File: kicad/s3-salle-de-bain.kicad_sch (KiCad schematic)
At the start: 22 parts, among them J1 Jack 3.5mm PJ320E, J2 USB-C, Q1 AO3401, SW1 Encodeur EC11, SW2 Switch mute, U1 ESP32-S3-DevKitC-1, U2 PCM5102 DAC, U3 PAM8403, U4 INMP441, U5 AMS1117-3.3

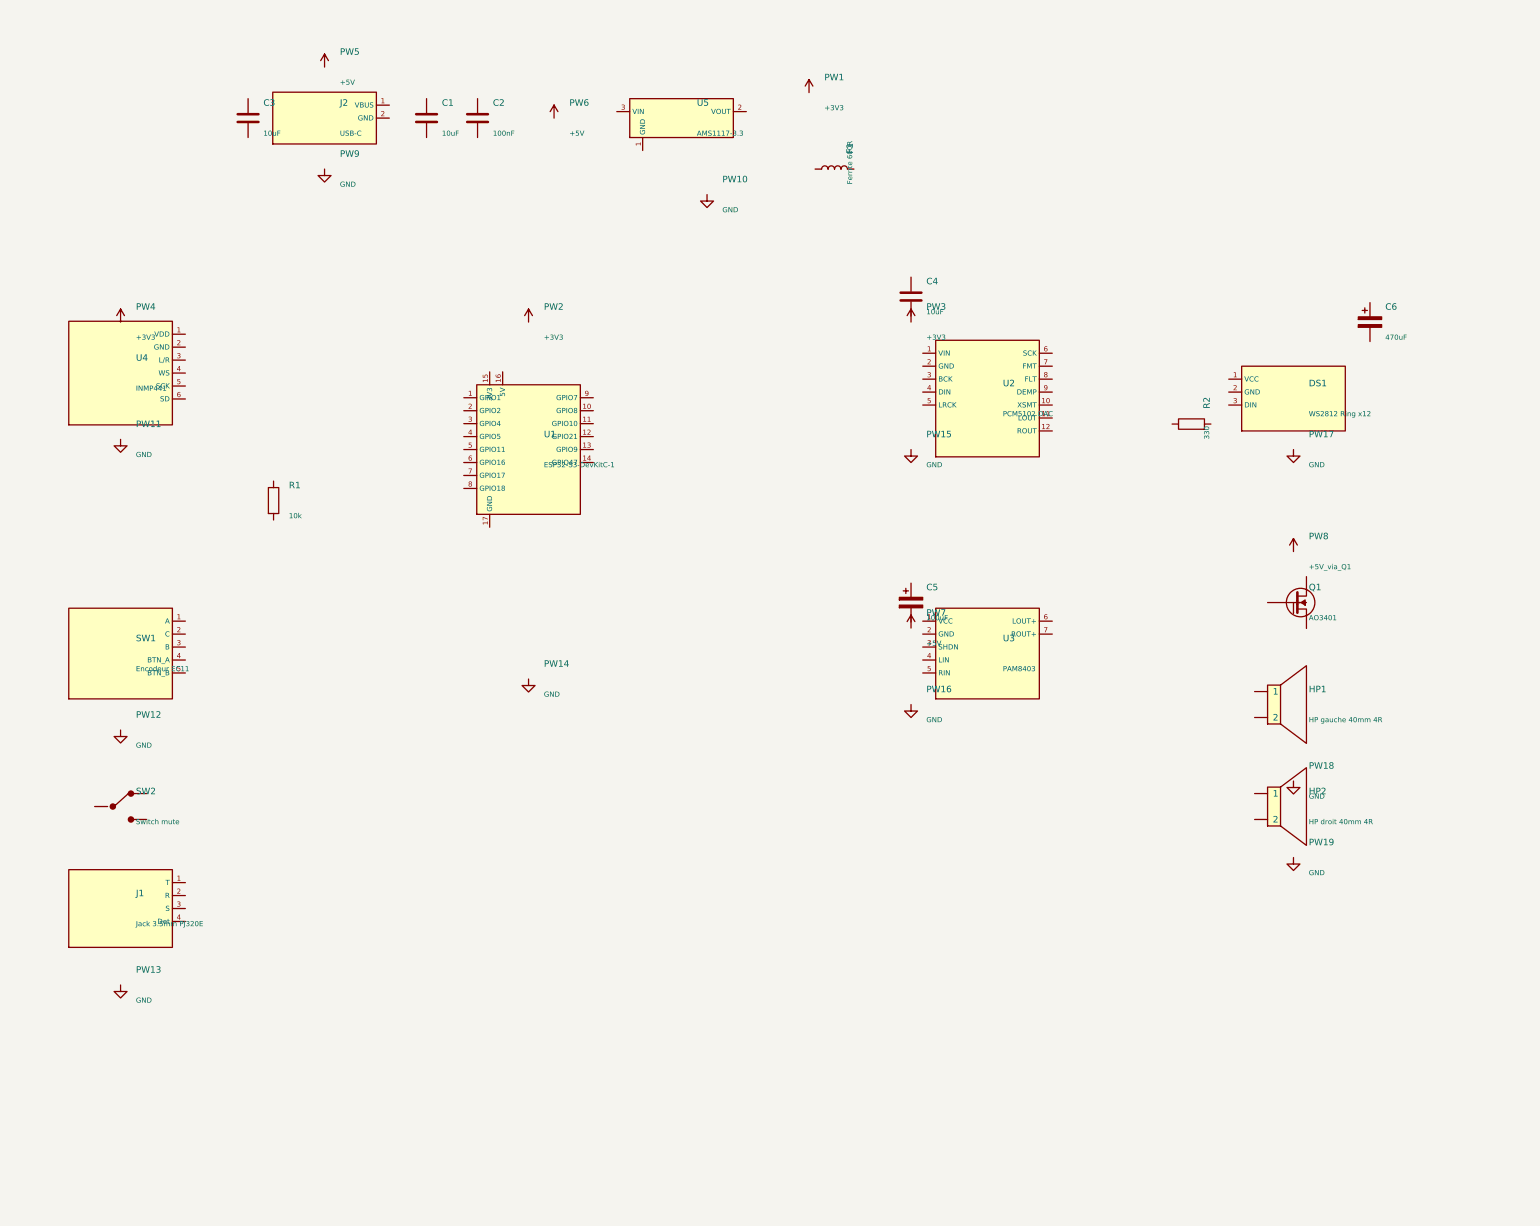
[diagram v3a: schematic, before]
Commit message: fix(kicad): real standard symbols (R/C/L/Q_PMOS/Speaker/power) + clean wiring
- Extract exact symbols from KiCad 10 libs (no lib_symbol_mismatch)
- Parse real pin positions (no off-grid, no unconnected endpoints)
- Grid-snapped placement, PWR_FLAG on each rail
- ERC: 216 -> 19 warnings (only cosmetic Local-lib notices)
- Verified with kicad-cli erc/pdf/svg export
- Official netlist: 24 nets, 22 components all connected
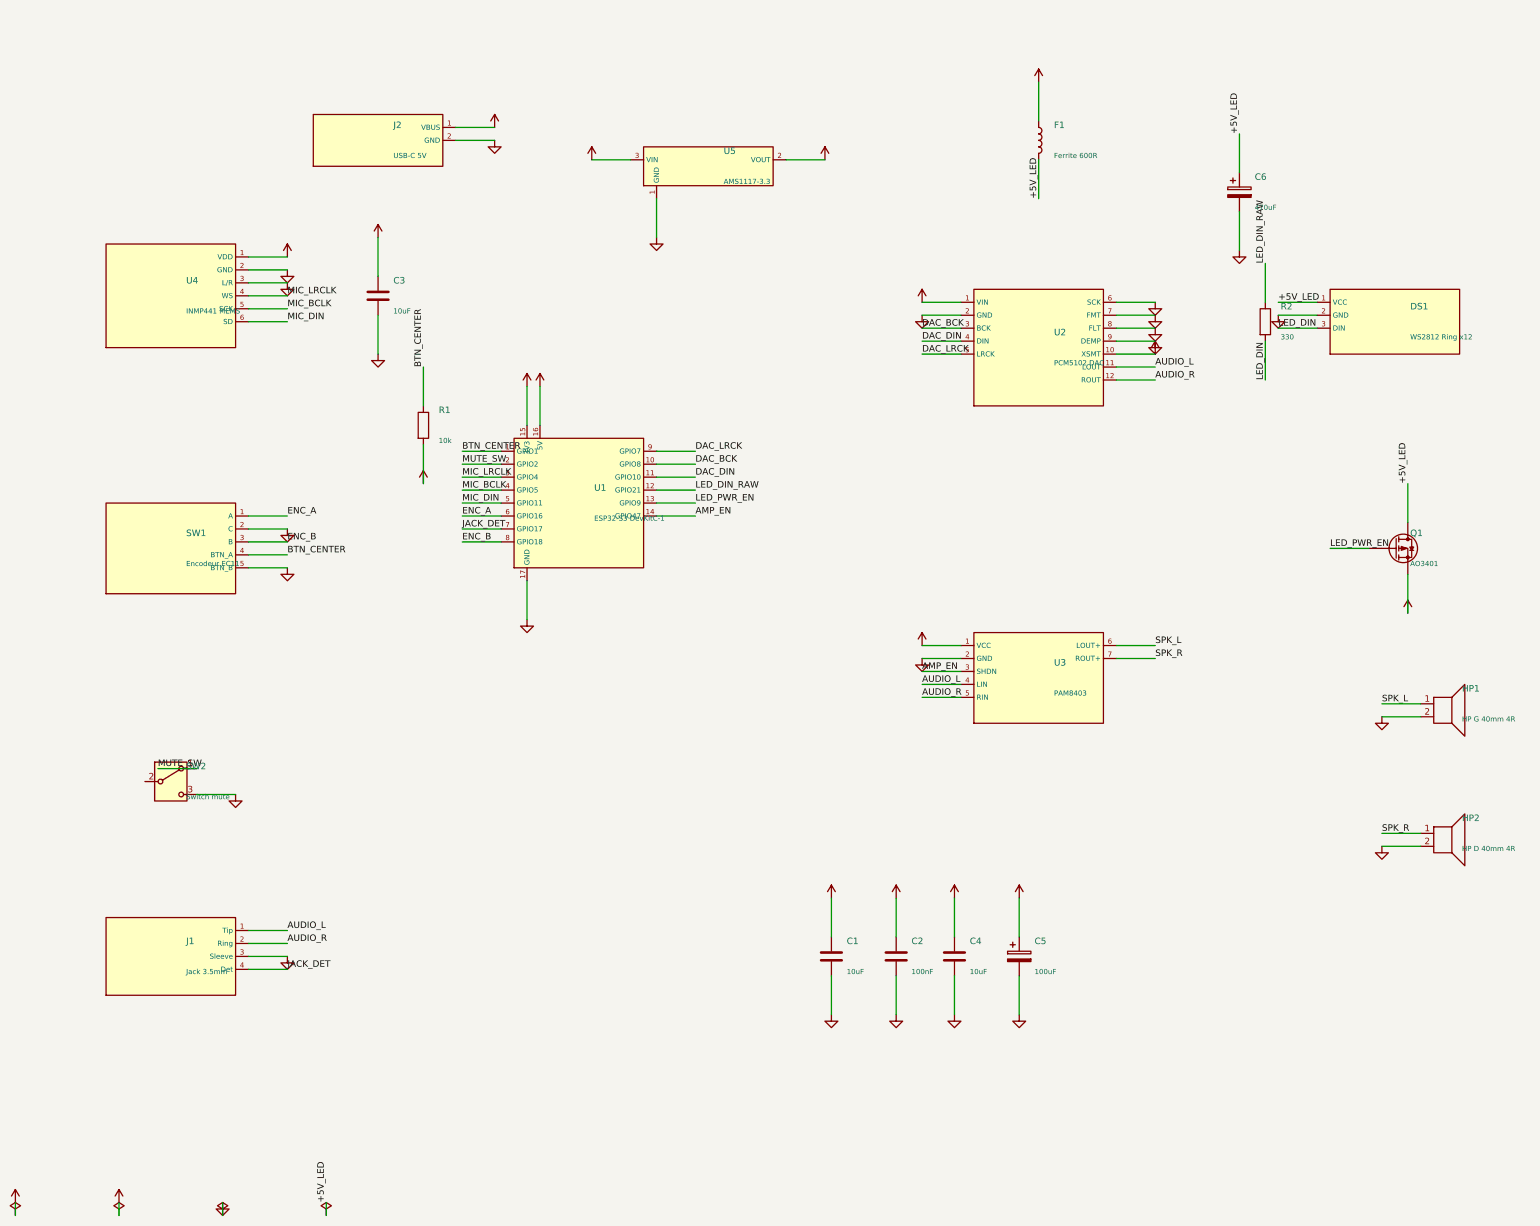
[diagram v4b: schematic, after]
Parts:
- removed C5: 100uF, symbol Device:CP
- removed C6: 470uF, symbol Device:CP
- removed Q1: AO3401, symbol Device:Q_PMOS_GSD
- added C5: 100uF, symbol Device:C_Polarized
- added C6: 470uF, symbol Device:C_Polarized
- added Q1: AO3401, symbol Device:Q_PMOS
- HP1: value HP gauche 40mm 4R -> HP G 40mm 4R
- HP2: value HP droit 40mm 4R -> HP D 40mm 4R
- J1: value Jack 3.5mm PJ320E -> Jack 3.5mm
- J2: value USB-C -> USB-C 5V
- U1: value ESP32-S3-DevKitC-1 -> ESP32-S3 DevKitC-1
- U4: value INMP441 -> INMP441 MEMS
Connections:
- net +3V3: now also C3.1, C4.1, R1.2, U1.15 (3V3), U2.1 (VIN), U2.10 (XSMT), U4.1 (VDD), U5.2 (VOUT)
- net +5V: now also C1.1, C2.1, F1.1, J2.1 (VBUS), U1.16 (5V), U3.1 (VCC), U5.3 (VIN), C5.1, Q1.S
- net GND: now also C1.2, C2.2, C3.2, C4.2, DS1.2 (GND), HP1.2, HP2.2, J1.3 (Sleeve), J2.2 (GND), SW1.2 (C), SW1.5 (BTN_B), SW2.3 (C), U1.17 (GND), U2.2 (GND), U2.6 (SCK), U2.7 (FMT), U2.8 (FLT), U2.9 (DEMP), U3.2 (GND), U4.2 (GND), U4.3 (L/R), U5.1 (GND), C5.2, C6.2
- net BTN_CENTER: now reaches U1.1 (GPIO1)
- net BTN_CENTER: now also R1.1, SW1.4 (BTN_A)
- net DAC_BCK: now reaches U1.10 (GPIO8)
- net DAC_BCK: now also U2.3 (BCK)
- net DAC_DIN: now reaches U1.11 (GPIO10)
- net DAC_DIN: now also U2.4 (DIN)
- net LED_DIN_RAW: now reaches U1.12 (GPIO21)
- net LED_DIN_RAW: now also R2.1
- net LED_PWR_EN: now reaches U1.13 (GPIO9)
- net LED_PWR_EN: now also Q1.G
- net AMP_EN: now reaches U1.14 (GPIO47)
- net AMP_EN: now also U3.3 (SHDN)
- net MUTE_SW: now reaches U1.2 (GPIO2)
- net MUTE_SW: now also SW2.1 (A)
- net MIC_LRCLK: now reaches U1.3 (GPIO4)
- net MIC_LRCLK: now also U4.4 (WS)
- net MIC_BCLK: now reaches U1.4 (GPIO5)
- net MIC_BCLK: now also U4.5 (SCK)
- net MIC_DIN: now reaches U1.5 (GPIO11)
- net MIC_DIN: now also U4.6 (SD)
- net ENC_A: now reaches U1.6 (GPIO16)
- net ENC_A: now also SW1.1 (A)
- net JACK_DET: now reaches U1.7 (GPIO17)
- net JACK_DET: now also J1.4 (Det)
- net ENC_B: now reaches U1.8 (GPIO18)
- net ENC_B: now also SW1.3 (B)
- net DAC_LRCK: now reaches U1.9 (GPIO7)
- net DAC_LRCK: now also U2.5 (LRCK)
- net SPK_R: now reaches HP2.1
- net SPK_R: now also U3.7 (ROUT+)
- net AUDIO_L: now reaches J1.1 (Tip)
- net AUDIO_L: now also U2.11 (LOUT), U3.4 (LIN)
- net AUDIO_R: now reaches J1.2 (Ring)
- net AUDIO_R: now also U2.12 (ROUT), U3.5 (RIN)
- net SPK_L: now reaches HP1.1
- net SPK_L: now also U3.6 (LOUT+)
- net +5V_LED: now reaches F1.2
- net +5V_LED: now also DS1.1 (VCC), C6.1, Q1.D
- net LED_DIN: now reaches R2.2
- net LED_DIN: now also DS1.3 (DIN)

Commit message: fix(pcb): real component footprints via pcbnew API (DRC clean)
- 22 real footprints from KiCad libs (SOT-223, SOT-23, EC11 encoder,
  PJ-320E jack, USB-C receptacle, SMD 0603/electrolytic, pin headers)
- 99 pads assigned to 23 nets, ratsnest ready to route
- DRC: 0 errors (edge clearance relaxed to 0.25mm for USB-C edge connector)
- Schematic symbols carry matching Footprint property (sch<->pcb linked)
- Verified with kicad-cli pcb drc + export
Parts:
- C1, C2, C3, C4: footprint (none) -> Capacitor_SMD:C_0603_1608Metric
- C5, C6: footprint (none) -> Capacitor_SMD:CP_Elec_5x5.3
- DS1: footprint (none) -> Connector_PinHeader_2.54mm:PinHeader_1x03_P2.54mm_Vertical
- F1: footprint (none) -> Inductor_SMD:L_0805_2012Metric
- HP1, HP2: footprint (none) -> Connector_PinHeader_2.54mm:PinHeader_1x02_P2.54mm_Vertical
- J1: footprint (none) -> Connector_Audio:Jack_3.5mm_PJ320E_Horizontal
- J2: footprint (none) -> Connector_USB:USB_C_Receptacle_Amphenol_12401610E4-2A
- Q1: footprint (none) -> Package_TO_SOT_SMD:SOT-23
- R1, R2: footprint (none) -> Resistor_SMD:R_0603_1608Metric
- SW1: footprint (none) -> Rotary_Encoder:RotaryEncoder_Alps_EC11E-Switch_Vertical_H20mm
- SW2: footprint (none) -> Button_Switch_THT:SW_DIP_SPSTx01_Slide_9.78x4.72mm_W7.62mm_P2.54mm
- U1: footprint (none) -> Connector_PinHeader_2.54mm:PinHeader_2x11_P2.54mm_Vertical
- U2: footprint (none) -> Connector_PinHeader_2.54mm:PinHeader_2x06_P2.54mm_Vertical
- U3: footprint (none) -> Connector_PinHeader_2.54mm:PinHeader_1x07_P2.54mm_Vertical
- U4: footprint (none) -> Connector_PinHeader_2.54mm:PinHeader_1x06_P2.54mm_Vertical
- U5: footprint (none) -> Package_TO_SOT_SMD:SOT-223-3_TabPin2

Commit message: fix(pcb): real ESP32-S3-DevKitC footprint (official Espressif)
- Download official Espressif ESP32-S3-DevKitC.kicad_mod (44 pads, 2x22)
- Map nets to exact GPIO pads per Espressif silk pinout
- Register Espressif.pretty in fp-lib-table
- Reposition all components around the larger module footprint
- DRC: 0 errors
- Schematic U1 footprint property -> Espressif:ESP32-S3-DevKitC
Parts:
- U1: footprint Connector_PinHeader_2.54mm:PinHeader_2x11_P2.54mm_Vertical -> Espressif:ESP32-S3-DevKitC

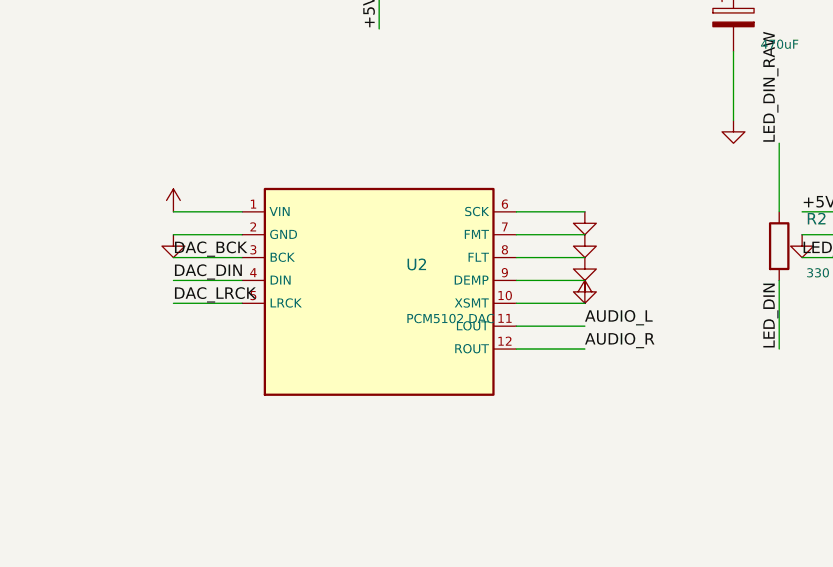
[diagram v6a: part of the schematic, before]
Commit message: fix(pcb): real GY-PCM5102 module footprint (1x11 header + L/G/R)
- Custom footprint matching the WCMCU/GY-PCM5102 board (31.8x23.8mm)
- Pin order XMT FMT LCK DIN BCK SCL DMP FLT GND 3V3 VCC + L/G/R line-out
- Net mapping per module silk (SCL/DMP/FLT/FMT->GND, XMT->3V3)
- Schematic U2 symbol + footprint property updated to match
- Register Modules.pretty in fp-lib-table
- DRC: 0 errors
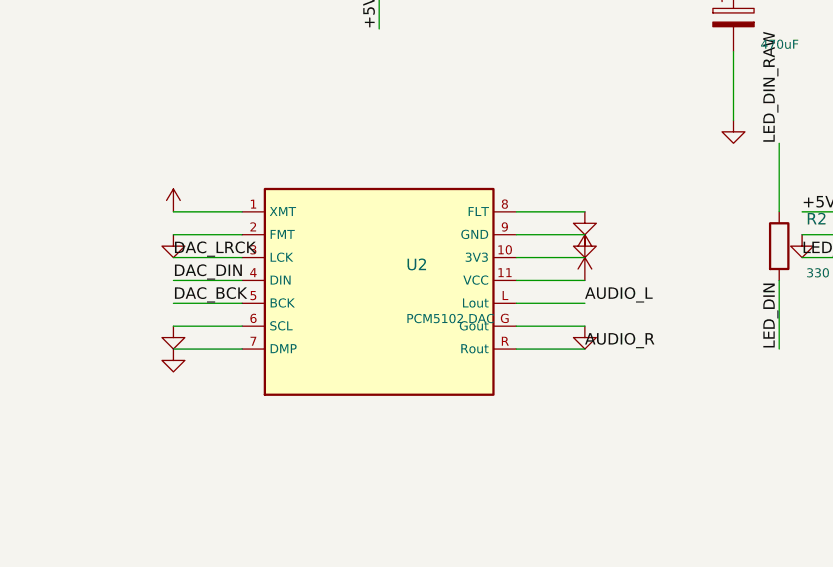
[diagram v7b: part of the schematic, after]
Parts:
- U2: footprint Connector_PinHeader_2.54mm:PinHeader_2x06_P2.54mm_Vertical -> Modules:GY-PCM5102
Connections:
- net +3V3: now also U2.11 (VCC)
- net AUDIO_L: now also U2.L (Lout); no longer U2.11 (LOUT)
- net AUDIO_R: now also U2.R (Rout); no longer U2.12 (ROUT)
- net DAC_BCK: now also U2.5 (BCK); no longer U2.3 (BCK)
- net DAC_LRCK: now also U2.3 (LCK); no longer U2.5 (LRCK)
- net GND: now also U2.G (Gout)

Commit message: fix(pcb): real INMP441 + PAM8403 module footprints (from photos)
- GY-INMP441 round footprint (2x3: L/R WS SCK / SD VDD GND)
- PAM8403-mini footprint (BTL out L-/L+/R-/R+, audio in L/G/R, power +/-)
- Speakers now wired differential (SPK_L+/L-, SPK_R+/R-) not to GND
- Add Q2 P-MOSFET amp power-gate (GPIO47 enables PAM8403, no SHDN on module)
- New +5V_AMP gated rail
- Schematic symbols + footprint properties updated to match
- Board widened to 145x108mm, DRC: 0 errors
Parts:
- added Q2: AO3401 (amp gate), Package_TO_SOT_SMD:SOT-23, symbol Device:Q_PMOS
- Q1: value AO3401 -> AO3401 (LED gate)
- U3: footprint Connector_PinHeader_2.54mm:PinHeader_1x07_P2.54mm_Vertical -> Modules:PAM8403-mini
- U4: footprint Connector_PinHeader_2.54mm:PinHeader_1x06_P2.54mm_Vertical -> Modules:GY-INMP441
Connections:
- net +3V3: now also U4.5 (VDD); no longer U4.1 (VDD)
- net +5V: now also Q2.S; no longer U3.1 (VCC)
- net AMP_EN: now also Q2.G; no longer U3.3 (SHDN)
- net AUDIO_L: now also U3.LI (Lin); no longer U3.4 (LIN)
- net AUDIO_R: now also U3.RI (Rin); no longer U3.5 (RIN)
- net GND: now also U3.GI (Gin), U3.V- (GND), U4.1 (L/R), U4.6 (GND); no longer HP1.2, HP2.2, U3.2 (GND), U4.2 (GND), U4.3 (L/R)
- net MIC_BCLK: now also U4.3 (SCK); no longer U4.5 (SCK)
- net MIC_DIN: now also U4.4 (SD); no longer U4.6 (SD)
- net MIC_LRCLK: now also U4.2 (WS); no longer U4.4 (WS)
- net SPK_L renamed SPK_L+
- net SPK_L+: now also U3.L+; no longer U3.6 (LOUT+)
- net SPK_R renamed SPK_R+
- net SPK_R+: now also U3.R+; no longer U3.7 (ROUT+)
- new net +5V_AMP: Q2.D, U3.V+
- new net SPK_L-: HP1.2, U3.L-
- new net SPK_R-: HP2.2, U3.R-
